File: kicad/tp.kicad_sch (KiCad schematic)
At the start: 16 parts, among them J1 HM10_Header, J2 MAX30102_Header, SW1 SWITCH_MODE, SW2 ALARM_OFF, U1 STM32F103RBTx

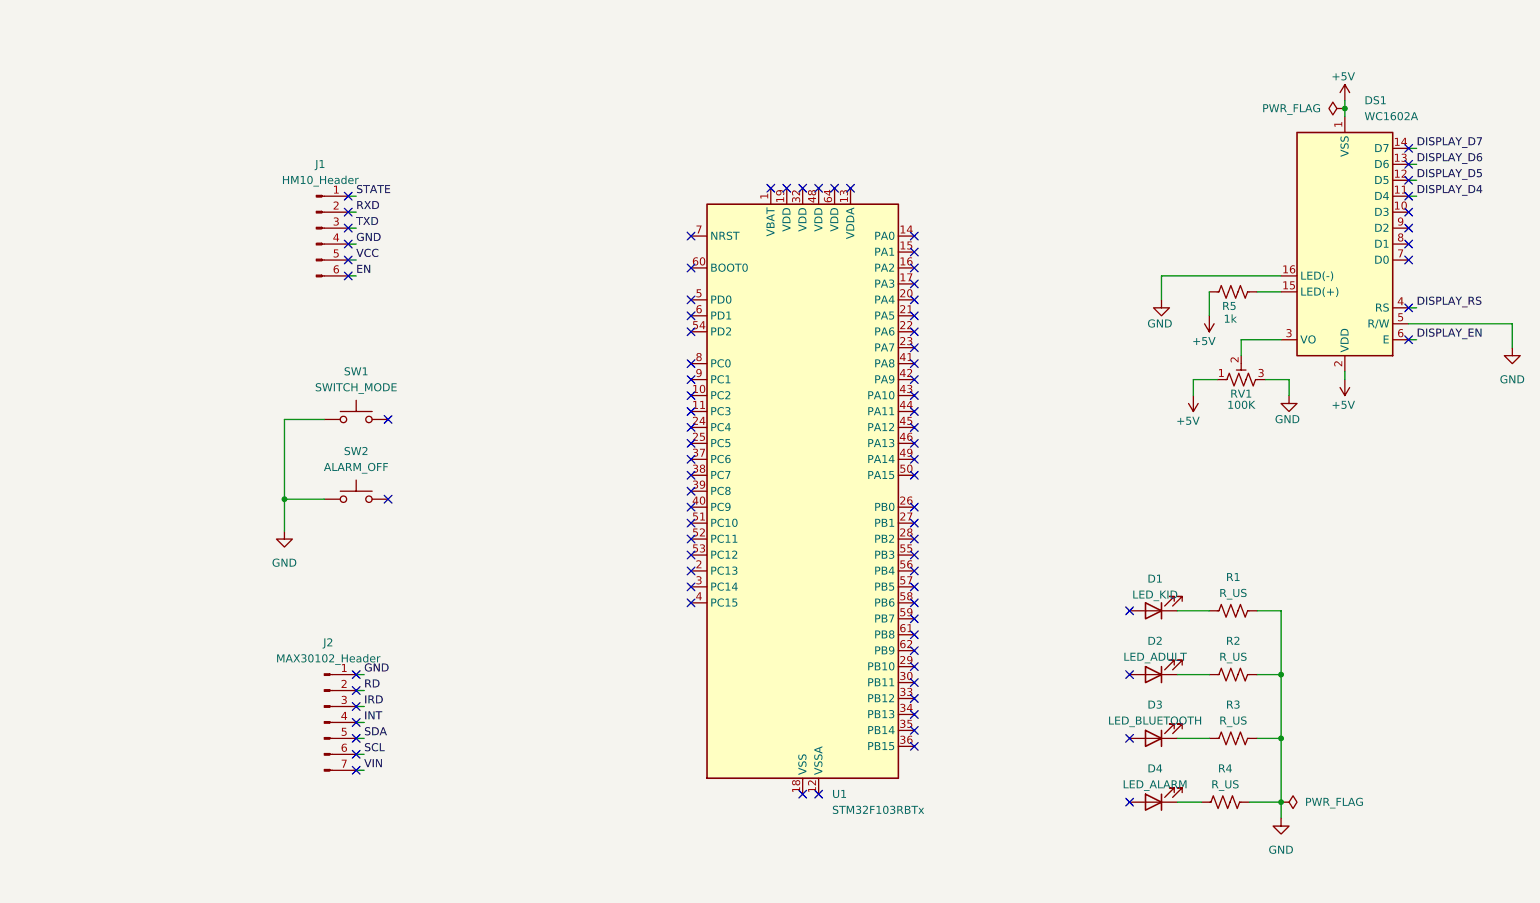
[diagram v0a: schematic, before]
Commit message: feat(sch): agrega symbol, footprint, y model de la NUCLEO-F103RB
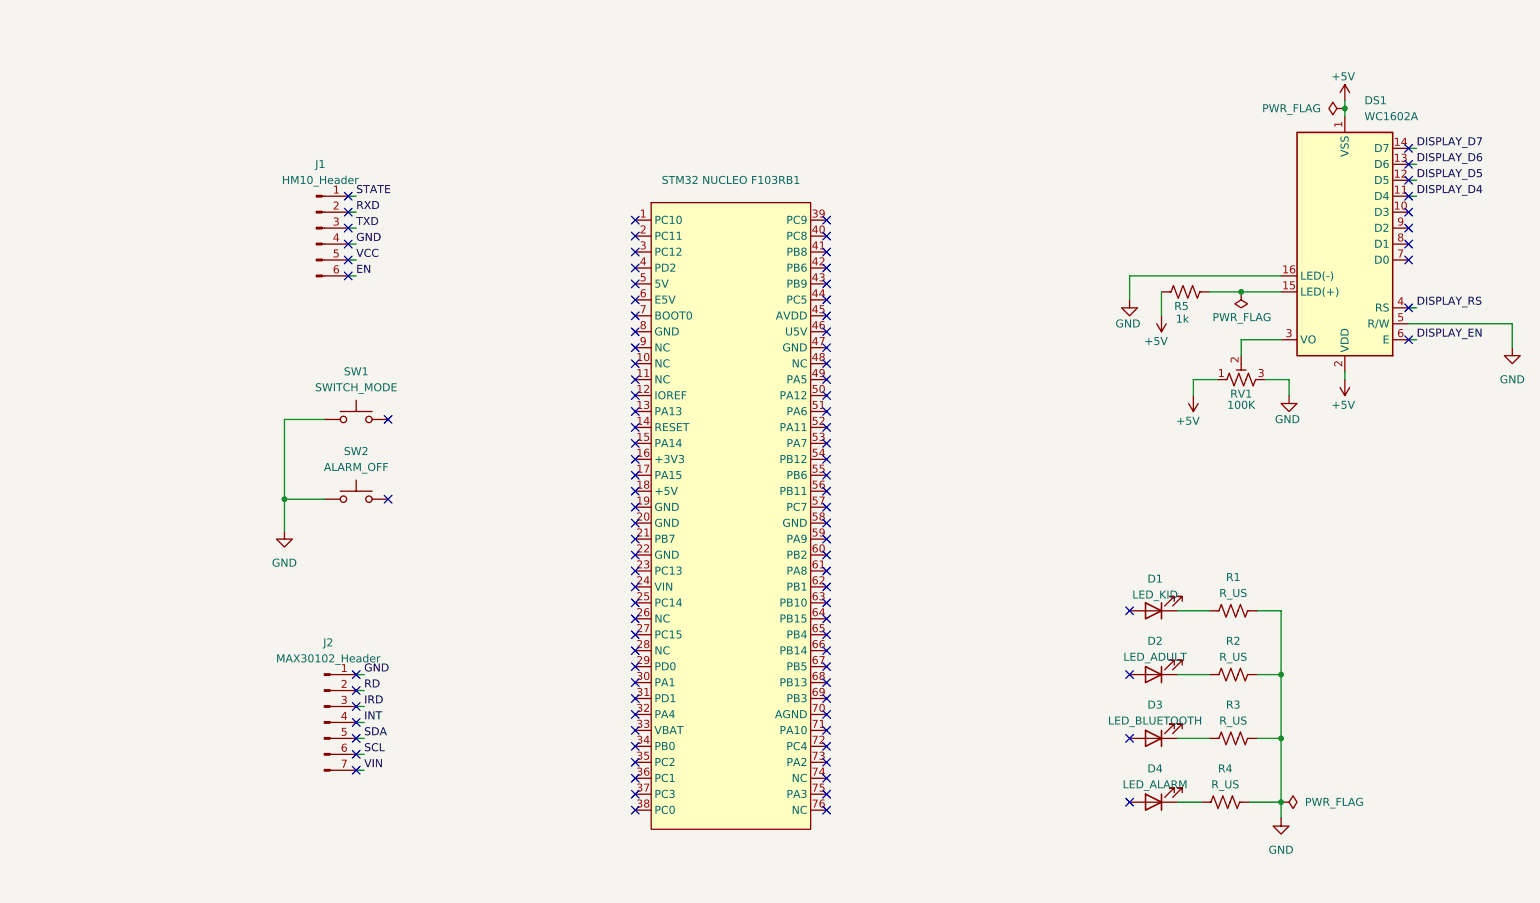
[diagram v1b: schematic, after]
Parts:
- removed U1: STM32F103RBTx, Package_QFP:LQFP-64_10x10mm_P0.5mm, symbol MCU_ST_STM32F1:STM32F103RBTx
- added STM32 NUCLEO F103RB1: ~, symbol STM32_NUCLEO:NUCLEO-F103RB
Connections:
- no-connect marks 90 -> 105
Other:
- moved on the sheet: R5

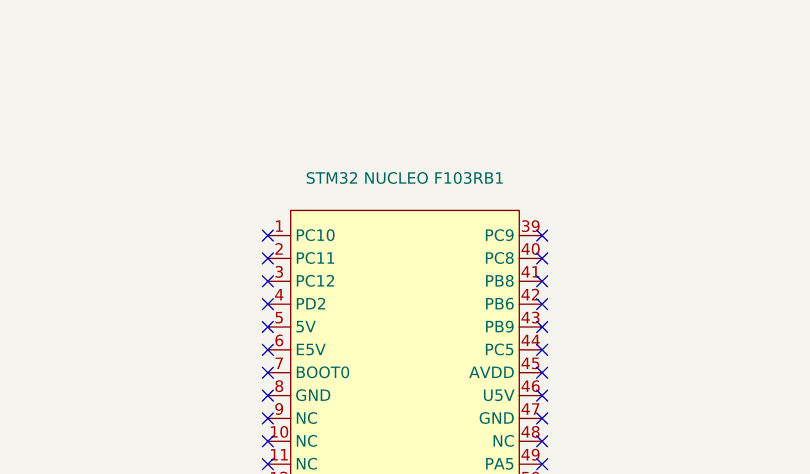
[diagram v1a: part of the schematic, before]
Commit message: fix(sch): actualizo campos del symbol de la nucleo
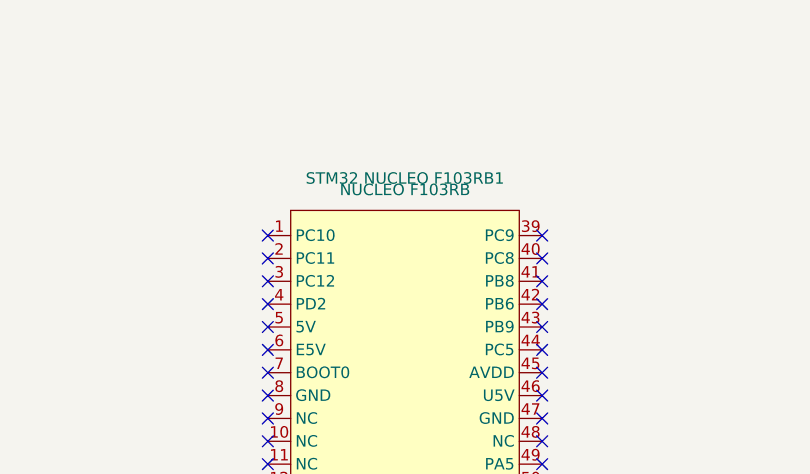
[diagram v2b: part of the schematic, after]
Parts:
- STM32 NUCLEO F103RB1: value ~ -> NUCLEO F103RB; footprint (none) -> STM32:NUCLEO F103RB
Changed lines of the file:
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@@
 			)
 		)
-		(property "Value" "~"
+		(property "Value" "NUCLEO F103RB"
 			(at 137.16 45.72 0)
 			(effects
@@
 			)
 		)
-		(property "Footprint" ""
+		(property "Footprint" "STM32:NUCLEO F103RB"
 			(at 137.16 96.52 0)
 			(effects
@@
 			)
 		)
-		(property "Datasheet" ""
+		(property "Datasheet" "https://www.st.com/resource/en/user_manual/um1724-stm32-nucleo64-boards-mb1136-stmicroelectronics.pdf"
 			(at 137.16 96.52 0)
 			(effects
@@
 			)
 		)
-		(property "Description" ""
+		(property "Description" "STM32 NUCLEO F103RB Board"
 			(at 137.16 96.52 0)
 			(effects

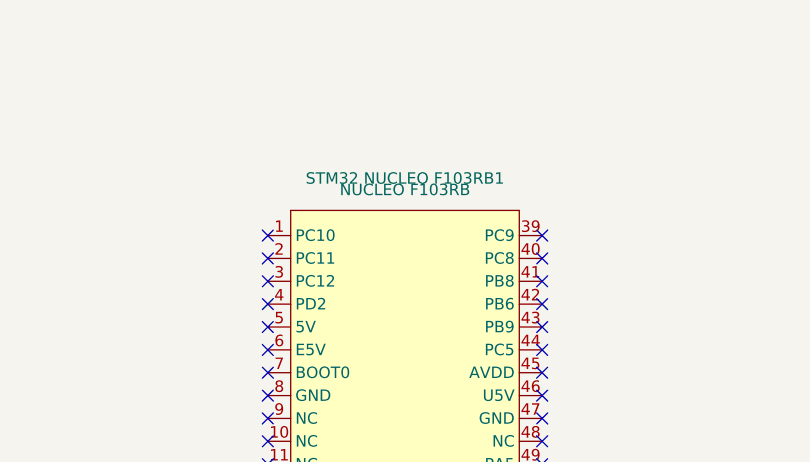
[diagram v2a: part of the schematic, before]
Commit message: fix(sch): elimino error de ERC en el symbol de nucleo
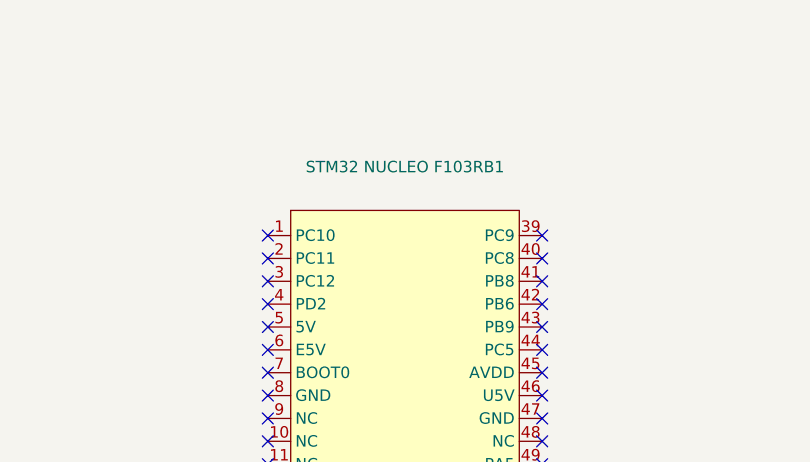
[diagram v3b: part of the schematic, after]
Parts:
- STM32 NUCLEO F103RB1: value NUCLEO F103RB -> ~; footprint STM32:NUCLEO F103RB -> (none)
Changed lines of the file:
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@@
-	)
-	(symbol
-		(lib_name "NUCLEO-F103RB_1")
-		(lib_id "STM32_NUCLEO:NUCLEO-F103RB")
-		(at 137.16 96.52 0)
-		(unit 1)
-		(exclude_from_sim no)
-		(in_bom yes)
-		(on_board yes)
-		(dnp no)
-		(fields_autoplaced yes)
-		(property "Reference" "STM32 NUCLEO F103RB1"
-			(at 137.16 44.45 0)
-			(effects
-				(font
-					(size 1.27 1.27)
-				)
-			)
-		)
-		(property "Value" "NUCLEO F103RB"
-			(at 137.16 45.72 0)
-			(effects
-				(font
-					(size 1.27 1.27)
-				)
-			)
-		)
-		(property "Footprint" "STM32:NUCLEO F103RB"
-			(at 137.16 96.52 0)
-			(effects
-				(font
-					(size 1.27 1.27)
-				)
-				(hide yes)
-			)
-		)
-		(property "Datasheet" "https://www.st.com/resource/en/user_manual/um1724-stm32-nucleo64-boards-mb1136-stmicroelectronics.pdf"
-			(at 137.16 96.52 0)
-			(effects
-				(font
-					(size 1.27 1.27)
-				)
-				(hide yes)
-			)
-		)
-		(property "Description" "STM32 NUCLEO F103RB Board"
-			(at 137.16 96.52 0)
-			(effects
-				(font
-					(size 1.27 1.27)
-				)
-				(hide yes)
-			)
-		)
-		(pin "21"
-		)
-		(pin "22"
-		)
-		(pin "55"
-		)
-		(pin "56"
-		)
-		(pin "57"
-		)
-		(pin "58"
-		)
-		(pin "23"
-		)
-		(pin "24"
-		)
-		(pin "75"
-		)
-		(pin "76"
-		)
-		(pin "2"
-		)
-		(pin "42"
-		)
-		(pin "10"
-		)
-		(pin "9"
-		)
-		(pin "8"
-		)
-		(pin "7"
-		)
-		(pin "6"
-		)
-		(pin "5"
-		)
-		(pin "4"
-		)
-		(pin "3"
-		)
-		(pin "1"
-		)
-		(pin "17"
-		)
-		(pin "16"
-		)
-		(pin "15"
-		)
-		(pin "14"
-		)
-		(pin "13"
-		)
-		(pin "12"
-		)
-		(pin "11"
-		)
-		(pin "18"
-		)
-		(pin "35"
-		)
-		(pin "36"
-		)
-		(pin "59"
-		)
-		(pin "60"
-		)
-		(pin "61"
-		)
-		(pin "62"
-		)
-		(pin "63"
-		)
-		(pin "64"
-		)
-		(pin "65"
-		)
-		(pin "66"
-		)
-		(pin "27"
-		)
-		(pin "28"
-		)
-		(pin "71"
-		)
-		(pin "72"
-		)
-		(pin "73"
-		)
-		(pin "74"
-		)
-		(pin "33"
-		)
-		(pin "34"
-		)
-		(pin "19"
-		)
-		(pin "20"
-		)
-		(pin "29"
-		)
-		(pin "30"
-		)
-		(pin "47"
-		)
-		(pin "48"
-		)
-		(pin "49"
-		)
-		(pin "50"
-		)
-		(pin "43"
-		)
-		(pin "44"
-		)
-		(pin "37"
-		)
-		(pin "38"
-		)
-		(pin "67"
-		)
-		(pin "68"
-		)
-		(pin "69"
-		)
-		(pin "70"
-		)
-		(pin "39"
-		)
-		(pin "40"
-		)
-		(pin "25"
-		)
-		(pin "26"
-		)
-		(pin "41"
-		)
-		(pin "45"
-		)
-		(pin "46"
-		)
-		(pin "31"
-		)
-		(pin "32"
-		)
-		(pin "51"
-		)
-		(pin "52"
-		)
-		(pin "53"
-		)
-		(pin "54"
-		)
-		(instances
-			(project ""
-				(path "/4321da81-5d44-4e9a-b537-a2876d1011a9"
-					(reference "STM32 NUCLEO F103RB1")
-					(unit 1)
-				)
-			)
-		)
 	)
 	(symbol
@@
 					(unit 1)
 				)
+			)
+		)
+	)
+	(symbol
+		(lib_id "STM32_NUCLEO:NUCLEO-F103RB")
+		(at 137.16 96.52 0)
+		(unit 1)
+		(exclude_from_sim no)
+		(in_bom yes)
+		(on_board yes)
+		(dnp no)
+		(fields_autoplaced yes)
+		(property "Reference" "STM32 NUCLEO F103RB1"
+			(at 137.16 43.18 0)
+			(effects
+				(font
+					(size 1.27 1.27)
+				)
+			)
+		)
+		(property "Value" "~"
+			(at 137.16 45.72 0)
+			(effects
+				(font
+					(size 1.27 1.27)
+				)
+			)
+		)
+		(property "Footprint" ""
+			(at 137.16 96.52 0)
+			(effects
+				(font
+					(size 1.27 1.27)
+				)
+				(hide yes)
+			)
+		)
+		(property "Datasheet" ""
+			(at 137.16 96.52 0)
+			(effects
+				(font
+					(size 1.27 1.27)
+				)
+				(hide yes)
+			)
+		)
+		(property "Description" ""
+			(at 137.16 96.52 0)
+			(effects
+				(font
+					(size 1.27 1.27)
+				)
+				(hide yes)
+			)
+		)
+		(pin "21"
+		)
+		(pin "75"
+		)
+		(pin "20"
+		)
+		(pin "63"
+		)
+		(pin "60"
+		)
+		(pin "61"
+		)
+		(pin "59"
+		)
+		(pin "58"
+		)
+		(pin "57"
+		)
+		(pin "70"
+		)
+		(pin "74"
+		)
+		(pin "72"
+		)
+		(pin "73"
+		)
+		(pin "71"
+		)
+		(pin "76"
+		)
+		(pin "2"
+		)
+		(pin "56"
+		)
+		(pin "23"
+		)
+		(pin "42"
+		)
+		(pin "44"
+		)
+		(pin "43"
+		)
+		(pin "32"
+		)
+		(pin "26"
+		)
+		(pin "50"
+		)
+		(pin "51"
+		)
+		(pin "52"
+		)
+		(pin "54"
+		)
+		(pin "53"
+		)
+		(pin "48"
+		)
+		(pin "49"
+		)
+		(pin "45"
+		)
+		(pin "35"
+		)
+		(pin "39"
+		)
+		(pin "33"
+		)
+		(pin "27"
+		)
+		(pin "28"
+		)
+		(pin "19"
+		)
+		(pin "25"
+		)
+		(pin "24"
+		)
+		(pin "65"
+		)
+		(pin "64"
+		)
+		(pin "29"
+		)
+		(pin "30"
+		)
+		(pin "22"
+		)
+		(pin "46"
+		)
+		(pin "47"
+		)
+		(pin "40"
+		)
+		(pin "41"
+		)
+		(pin "34"
+		)
+		(pin "62"
+		)
+		(pin "66"
+		)
+		(pin "31"
+		)
+		(pin "18"
+		)
+		(pin "69"
+		)
+		(pin "67"
+		)
+		(pin "68"
+		)
+		(pin "55"
+		)
+		(pin "36"
+		)
+		(pin "37"
+		)
+		(pin "17"
+		)
+		(pin "8"
+		)
+		(pin "7"
+		)
+		(pin "6"
+		)
+		(pin "5"
+		)
+		(pin "4"
+		)
+		(pin "3"
+		)
+		(pin "1"
+		)
+		(pin "38"
+		)
+		(pin "16"
+		)
+		(pin "15"
+		)
+		(pin "14"
+		)
+		(pin "13"
+		)
+		(pin "12"
+		)
+		(pin "11"
+		)
+		(pin "10"
+		)
+		(pin "9"
+		)
+		(instances
+			(project ""
+				(path "/4321da81-5d44-4e9a-b537-a2876d1011a9"
+					(reference "STM32 NUCLEO F103RB1")
+					(unit 1)
+				)

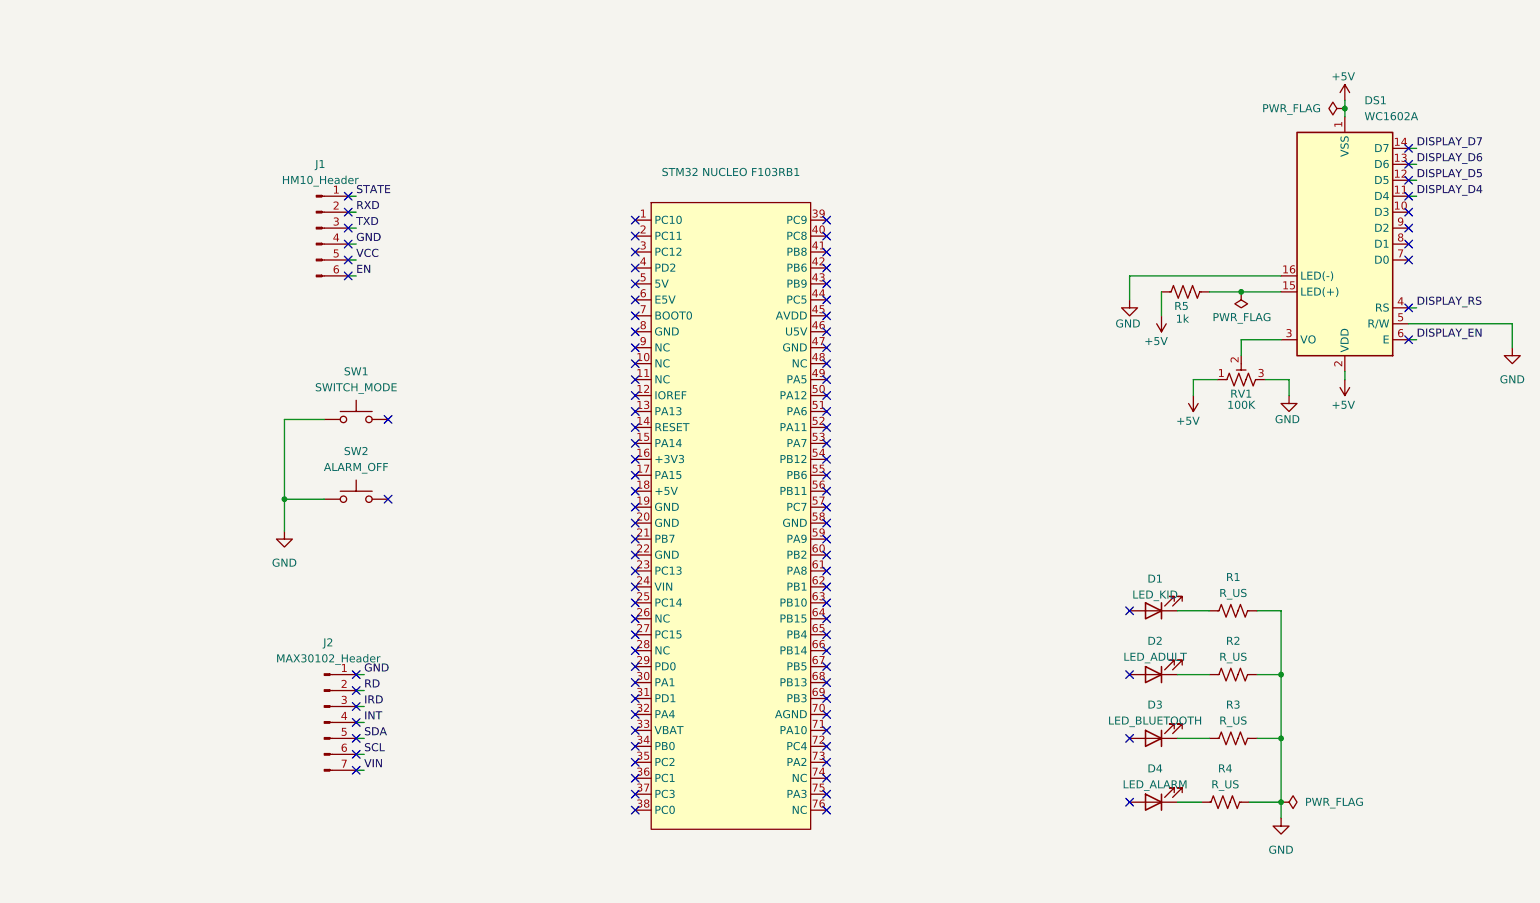
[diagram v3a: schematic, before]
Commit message: feat(sch): agrego symbol del hm10
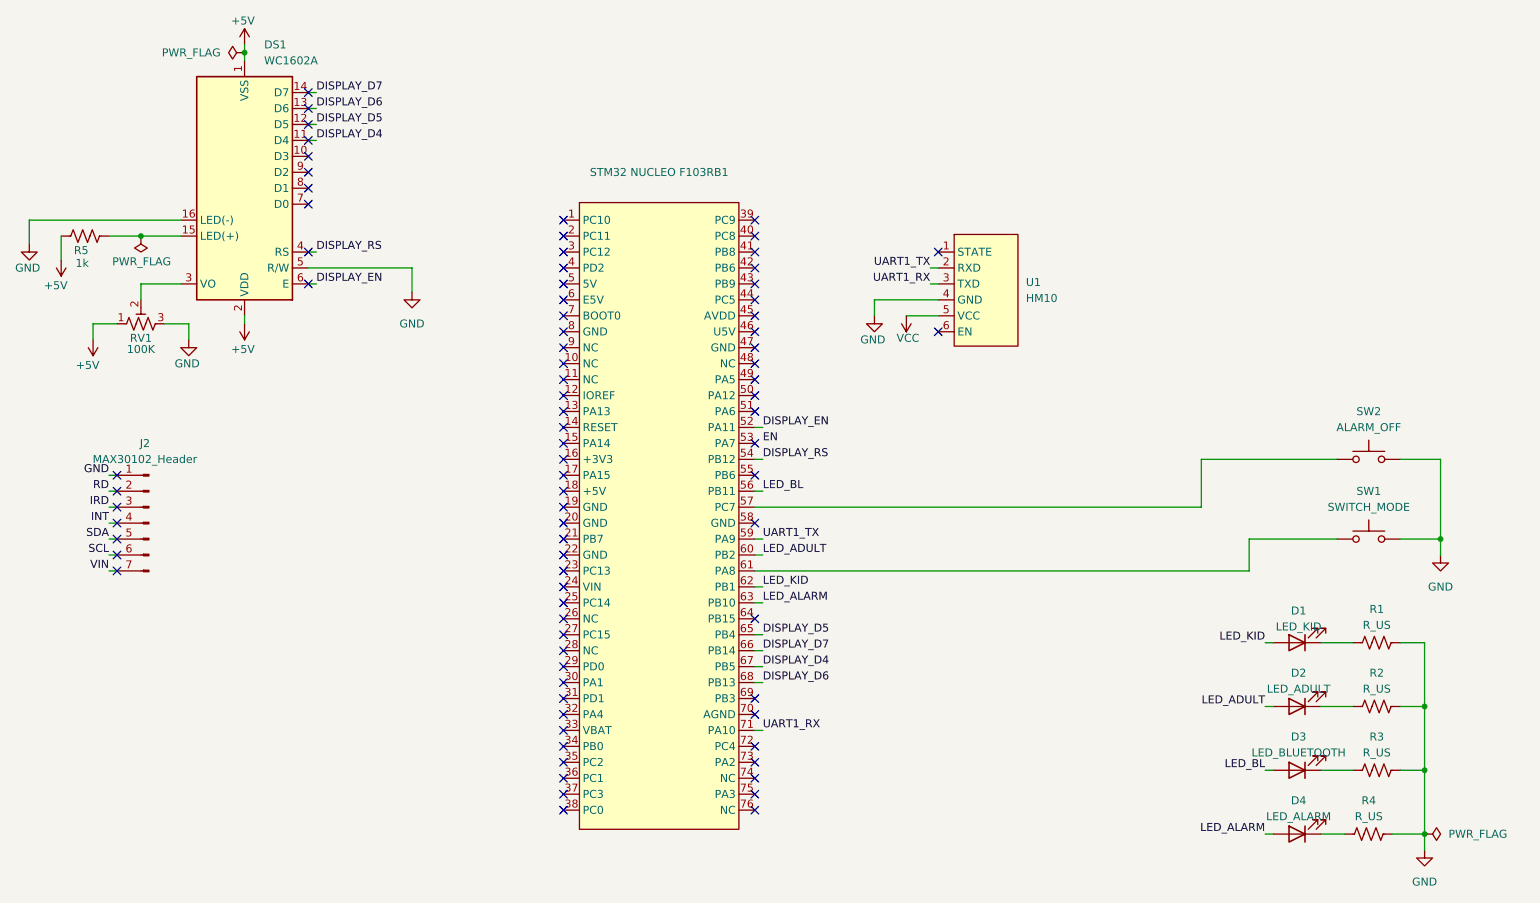
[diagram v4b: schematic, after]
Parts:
- removed J1: HM10_Header, symbol Connector:Conn_01x06_Pin
- added U1: HM10, symbol STM32_NUCLEO:HM10-Header
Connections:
- net DISPLAY_D4: now also STM32 NUCLEO F103RB1.67 (PB5)
- net DISPLAY_D5: now also STM32 NUCLEO F103RB1.65 (PB4)
- net DISPLAY_D6: now also STM32 NUCLEO F103RB1.68 (PB13)
- net DISPLAY_D7: now also STM32 NUCLEO F103RB1.66 (PB14)
- net DISPLAY_EN: now also STM32 NUCLEO F103RB1.52 (PA11)
- net DISPLAY_RS: now also STM32 NUCLEO F103RB1.54 (PB12)
- net GND: now also U1.4 (GND)
- net VCC: now also U1.5 (VCC)
- net at SW1.2: now also STM32 NUCLEO F103RB1.61 (PA8)
- net LED_KID: now reaches D1.2 (A)
- net LED_KID: now also STM32 NUCLEO F103RB1.62 (PB1)
- net at SW2.2: now also STM32 NUCLEO F103RB1.57 (PC7)
- net LED_ALARM: now reaches D4.2 (A)
- net LED_ALARM: now also STM32 NUCLEO F103RB1.63 (PB10)
- net LED_ADULT: now reaches D2.2 (A)
- net LED_ADULT: now also STM32 NUCLEO F103RB1.60 (PB2)
- net LED_BL: now reaches STM32 NUCLEO F103RB1.56 (PB11)
- net LED_BL: now also D3.2 (A)
- net UART1_TX: now reaches STM32 NUCLEO F103RB1.59 (PA9)
- net UART1_TX: now also U1.2 (RXD)
- net UART1_RX: now reaches STM32 NUCLEO F103RB1.71 (PA10)
- net UART1_RX: now also U1.3 (TXD)
- no-connect marks 105 -> 81
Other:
- moved on the sheet: D1, D2, D3, D4, DS1, J2, R1, R2, R3, R4, R5, RV1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
